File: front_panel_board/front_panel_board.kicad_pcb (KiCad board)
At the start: 2 copper layers, 70 x 35 mm, 13 parts, among them J1 Conn_01x02_Male, J2 Conn_02x05_Odd_Even, SW1 SW_Rotary12_Letter, SW2 SW_SPST

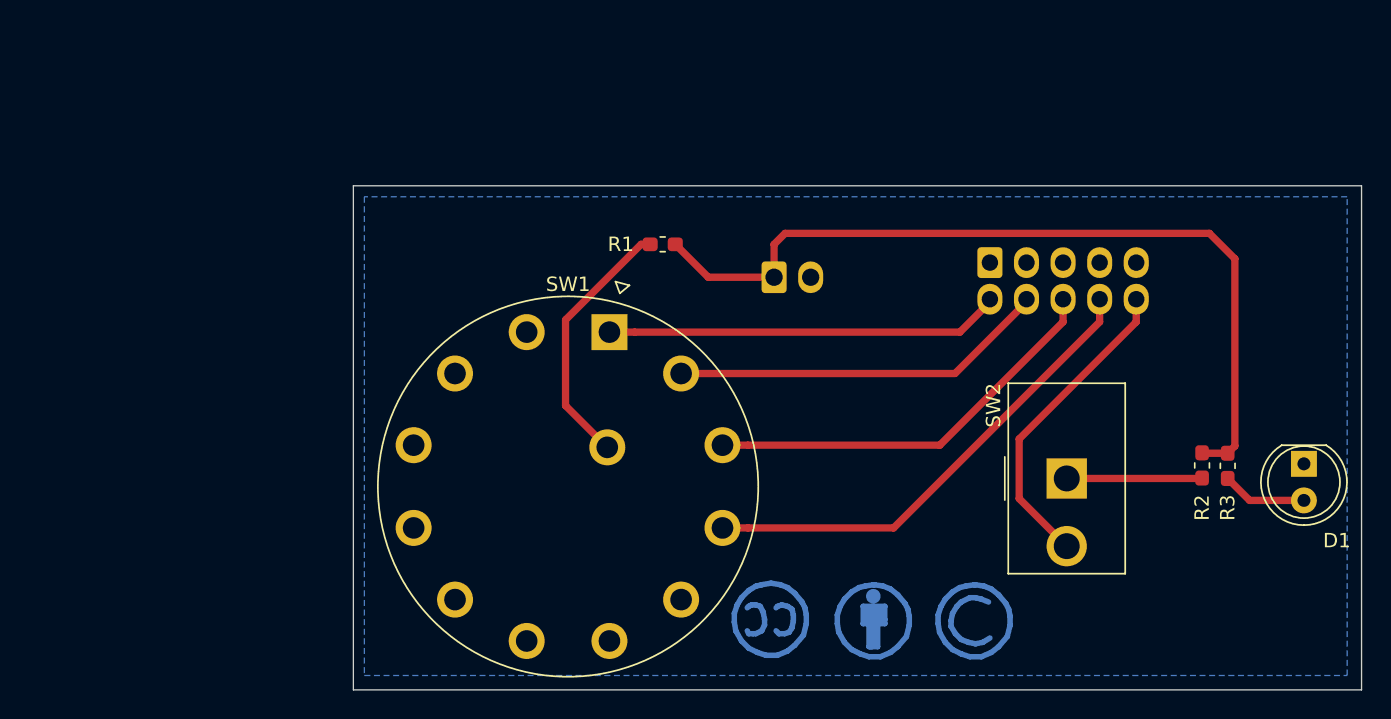
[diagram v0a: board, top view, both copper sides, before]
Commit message: update switch symbol/footprint, add second relay control connector, and re-layout (LED not laid out)
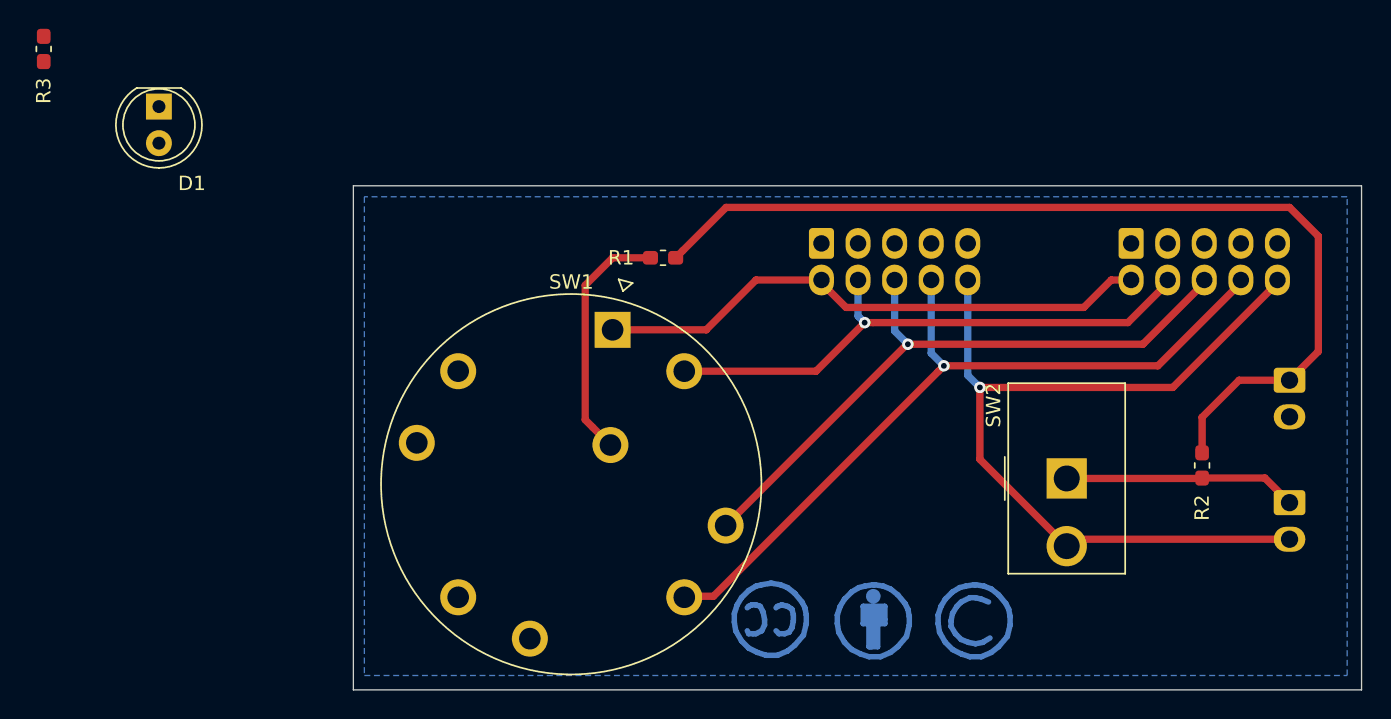
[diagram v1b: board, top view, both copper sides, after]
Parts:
- added J3: Conn_02x05_Odd_Even, Connector_Molex_C-Grid:Molex_C-Grid_70246-1001_2x05_P2.54mm_Vertical, B.Cu at (134.1, 54.8)
- added J4: Molex_SL_01x02_Male, Connector_Molex_SL:Molex_SL_A-70543-0001_1x02_P2.54mm_Vertical, B.Cu at (166.6, 72.8)
- J1: value Conn_01x02_Male -> Molex_SL_01x02_Male
- SW1: value SW_Rotary12_Letter -> SW_Rotary8_CK_A125xxxxCxx; footprint Button_Switch_THT_gkeeth:SW_Rotary12_C&K_A112xxxxCxx -> Button_Switch_THT_gkeeth:SW_Rotary8_CK_A125xxxxCxx
- moved R3 87.2 mm to (80.1, 41.3)
- moved D1 83.3 mm to (88.1, 45.3)
- moved REF** 45.5 mm to (121.1, 54.8)
- moved J1 36.5 mm to (166.6, 64.3), turned to 270 degrees
- moved J2 9.89 mm to (155.6, 54.8)
- moved R1 0.94 mm to (123.1, 55.8)
- moved SW1 0.27 mm to (119.6, 60.8)
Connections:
- SW1 pad 4: /input4_select -> /input3_select
- SW1 pad 5: Net-(SW1-Pad5) -> /input4_select
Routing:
- net /output_mute_select: track 21.9 -> 60.9 mm, vias 0 -> 1
- net /input4_select: track 33.7 -> 54.2 mm, vias 0 -> 1
- net /input3_select: track 28.8 -> 45.3 mm, vias 0 -> 1
- net /input2_select: track 26.2 -> 39.5 mm, vias 0 -> 1
- net /input1_select: track 27.5 -> 39.1 mm
- net Vrelay: track 58.6 -> 67.3 mm
- net Net-(J4-Pad1): track 9.41 -> 16.2 mm
- net Net-(D1-Pad2): track 5.93 -> 0.00 mm
- net Net-(R1-Pad2): track 18.1 -> 17.1 mm
